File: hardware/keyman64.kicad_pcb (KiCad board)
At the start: 2 copper layers, 80 x 64.7 mm, 33 parts, among them J1 POWER, P1 COMPUTER, P2 KEYBOARD, P3 USB, P4 SERIAL, P5 CONTROL, SW1 RESET, SW2 BOOT, U1 MT8808, U2 ATMEGA1284P-PU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

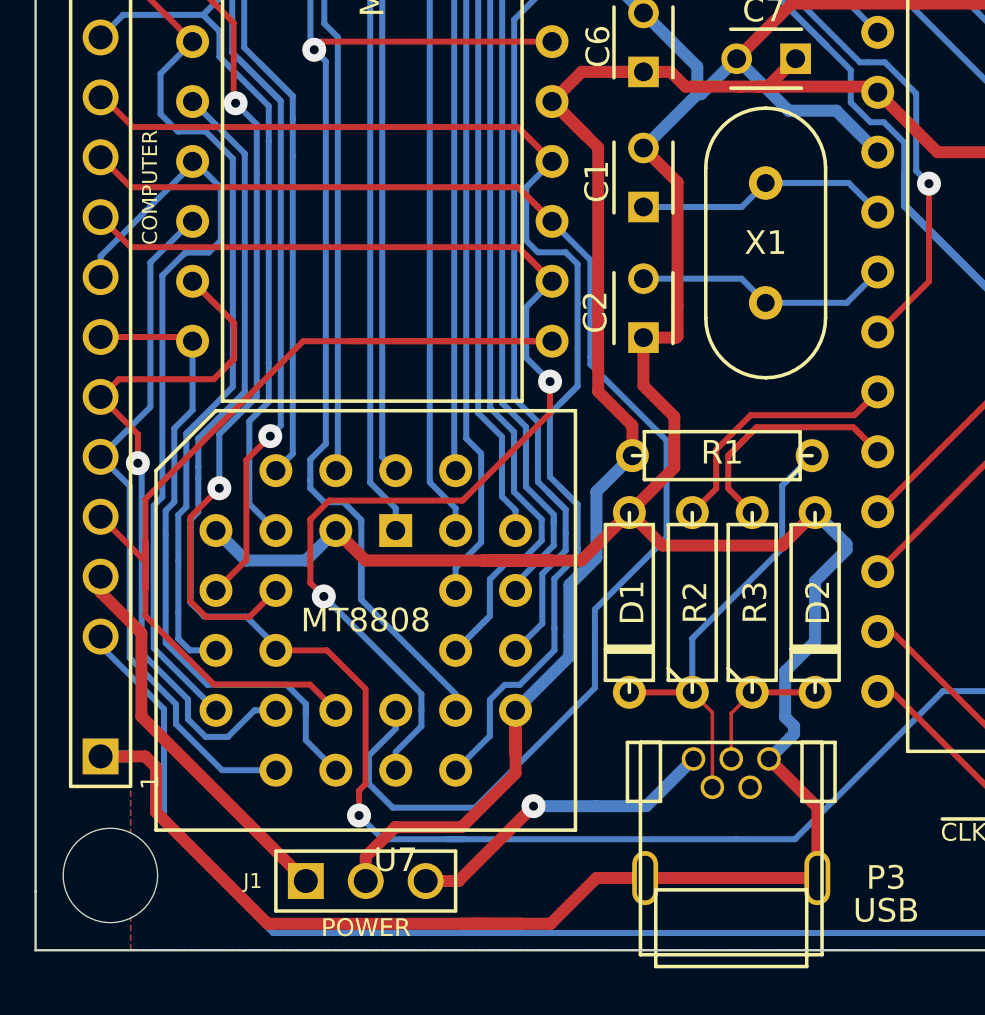
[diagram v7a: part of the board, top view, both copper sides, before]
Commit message: Hardware: Improved silkscreen, added component values
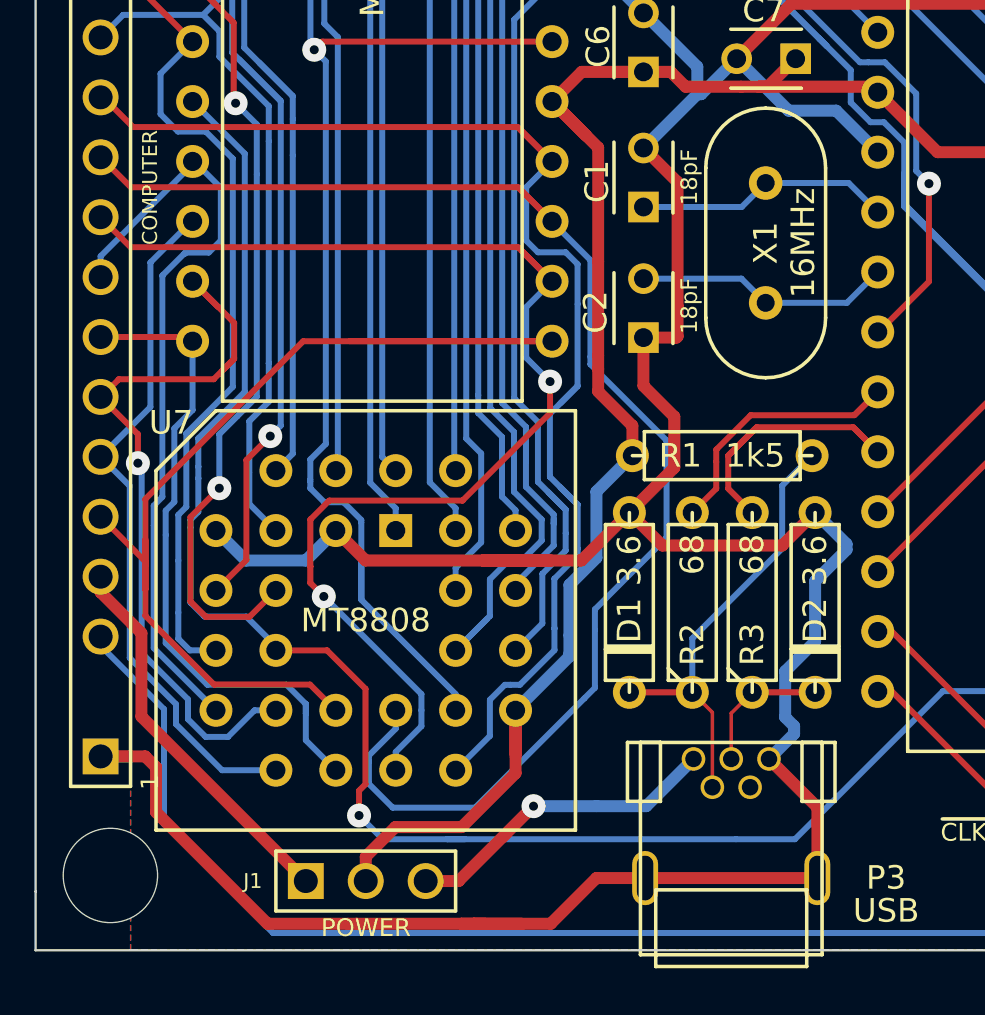
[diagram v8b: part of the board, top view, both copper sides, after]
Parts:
- D1, D2: value 3.6V -> 3.6
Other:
- board text added: "18pF"
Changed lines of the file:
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@@
-(kicad_pcb (version 4) (host pcbnew 4.0.1-stable)
+(kicad_pcb (version 4) (host pcbnew 4.0.2-stable)
   (general
     (links 171)
@@
     (area 104.572599 66.320199 184.657201 131.126701)
     (thickness 1.6)
-    (drawings 22)
+    (drawings 24)
     (tracks 1284)
     (zones 0)
@@
     (descr "Quartz boitier HC-49 Vertical")
     (tags "QUARTZ DEV")
-    (fp_text reference X1 (at 0 0.0005 180) (layer F.SilkS)
-      (effects (font (size 1 1) (thickness 0.15)))
-    )
-    (fp_text value 16MHz (at -6.6802 0.0386 180) (layer F.SilkS) hide
+    (fp_text reference X1 (at 0 0.0005 270) (layer F.SilkS)
+      (effects (font (size 1 1) (thickness 0.15)))
+    )
+    (fp_text value 16MHz (at 0 1.588 270) (layer F.SilkS)
       (effects (font (size 1 1) (thickness 0.15)))
     )
@@
     (descr "Support Plcc 28 pins, pads ronds")
     (tags PLCC)
-    (fp_text reference U7 (at 1.27 10.16) (layer F.SilkS)
+    (fp_text reference U7 (at -8.255 -8.382) (layer F.SilkS)
       (effects (font (size 1 1) (thickness 0.15)))
     )
@@
     (descr "Resitance 3 pas")
     (tags R)
-    (fp_text reference R1 (at 0 0.127 180) (layer F.SilkS)
-      (effects (font (size 1 1) (thickness 0.15)))
-    )
-    (fp_text value 1k5 (at 0 0.127 180) (layer F.Fab)
+    (fp_text reference R1 (at 1.778 0 360) (layer F.SilkS)
+      (effects (font (size 1 1) (thickness 0.15)))
+    )
+    (fp_text value 1k5 (at -1.397 0 180) (layer F.SilkS)
       (effects (font (size 1 1) (thickness 0.15)))
     )
@@
     (descr "Resitance 3 pas")
     (tags R)
-    (fp_text reference R2 (at 0 0.127 90) (layer F.SilkS)
-      (effects (font (size 1 1) (thickness 0.15)))
-    )
-    (fp_text value 68 (at 0 0.127 90) (layer F.Fab)
+    (fp_text reference R2 (at -1.778 0 90) (layer F.SilkS)
+      (effects (font (size 1 1) (thickness 0.15)))
+    )
+    (fp_text value 68 (at 2.032 0 90) (layer F.SilkS)
       (effects (font (size 1 1) (thickness 0.15)))
     )
@@
     (descr "Resitance 3 pas")
     (tags R)
-    (fp_text reference R3 (at 0 0.127 90) (layer F.SilkS)
-      (effects (font (size 1 1) (thickness 0.15)))
-    )
-    (fp_text value 68 (at 0 0.127 90) (layer F.Fab)
+    (fp_text reference R3 (at -1.778 0 90) (layer F.SilkS)
+      (effects (font (size 1 1) (thickness 0.15)))
+    )
+    (fp_text value 68 (at 2.032 0 90) (layer F.SilkS)
       (effects (font (size 1 1) (thickness 0.15)))
     )
@@
     (descr "Resitance 3 pas")
     (tags R)
-    (fp_text reference D1 (at 0 0.127 90) (layer F.SilkS)
-      (effects (font (size 1 1) (thickness 0.15)))
-    )
-    (fp_text value 3.6V (at 0 0.127 90) (layer F.Fab)
+    (fp_text reference D1 (at -0.762 0 90) (layer F.SilkS)
+      (effects (font (size 1 1) (thickness 0.15)))
+    )
+    (fp_text value 3.6 (at 1.778 0 90) (layer F.SilkS)
       (effects (font (size 1 1) (thickness 0.15)))
     )
@@
     (descr "Resitance 3 pas")
     (tags R)
-    (fp_text reference D2 (at 0 0.127 90) (layer F.SilkS)
-      (effects (font (size 1 1) (thickness 0.15)))
-    )
-    (fp_text value 3.6V (at 0 0.127 90) (layer F.Fab)
+    (fp_text reference D2 (at -0.762 0 90) (layer F.SilkS)
+      (effects (font (size 1 1) (thickness 0.15)))
+    )
+    (fp_text value 3.6 (at 1.778 0 90) (layer F.SilkS)
       (effects (font (size 1 1) (thickness 0.15)))
     )
@@
       (net 75 /~RESET))
   )
+  (gr_text 18pF (at 132.334 98.298 90) (layer F.SilkS)
+    (effects (font (size 0.7 0.7) (thickness 0.15)))
+  )
+  (gr_text 18pF (at 132.334 103.759 90) (layer F.SilkS)
+    (effects (font (size 0.7 0.7) (thickness 0.15)))
+  )
   (gr_line (start 118.618 113.284) (end 118.618 129.54) (angle 90) (layer Dwgs.User) (width 0.2))
